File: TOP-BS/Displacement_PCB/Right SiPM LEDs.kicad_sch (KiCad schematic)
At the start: 36 parts

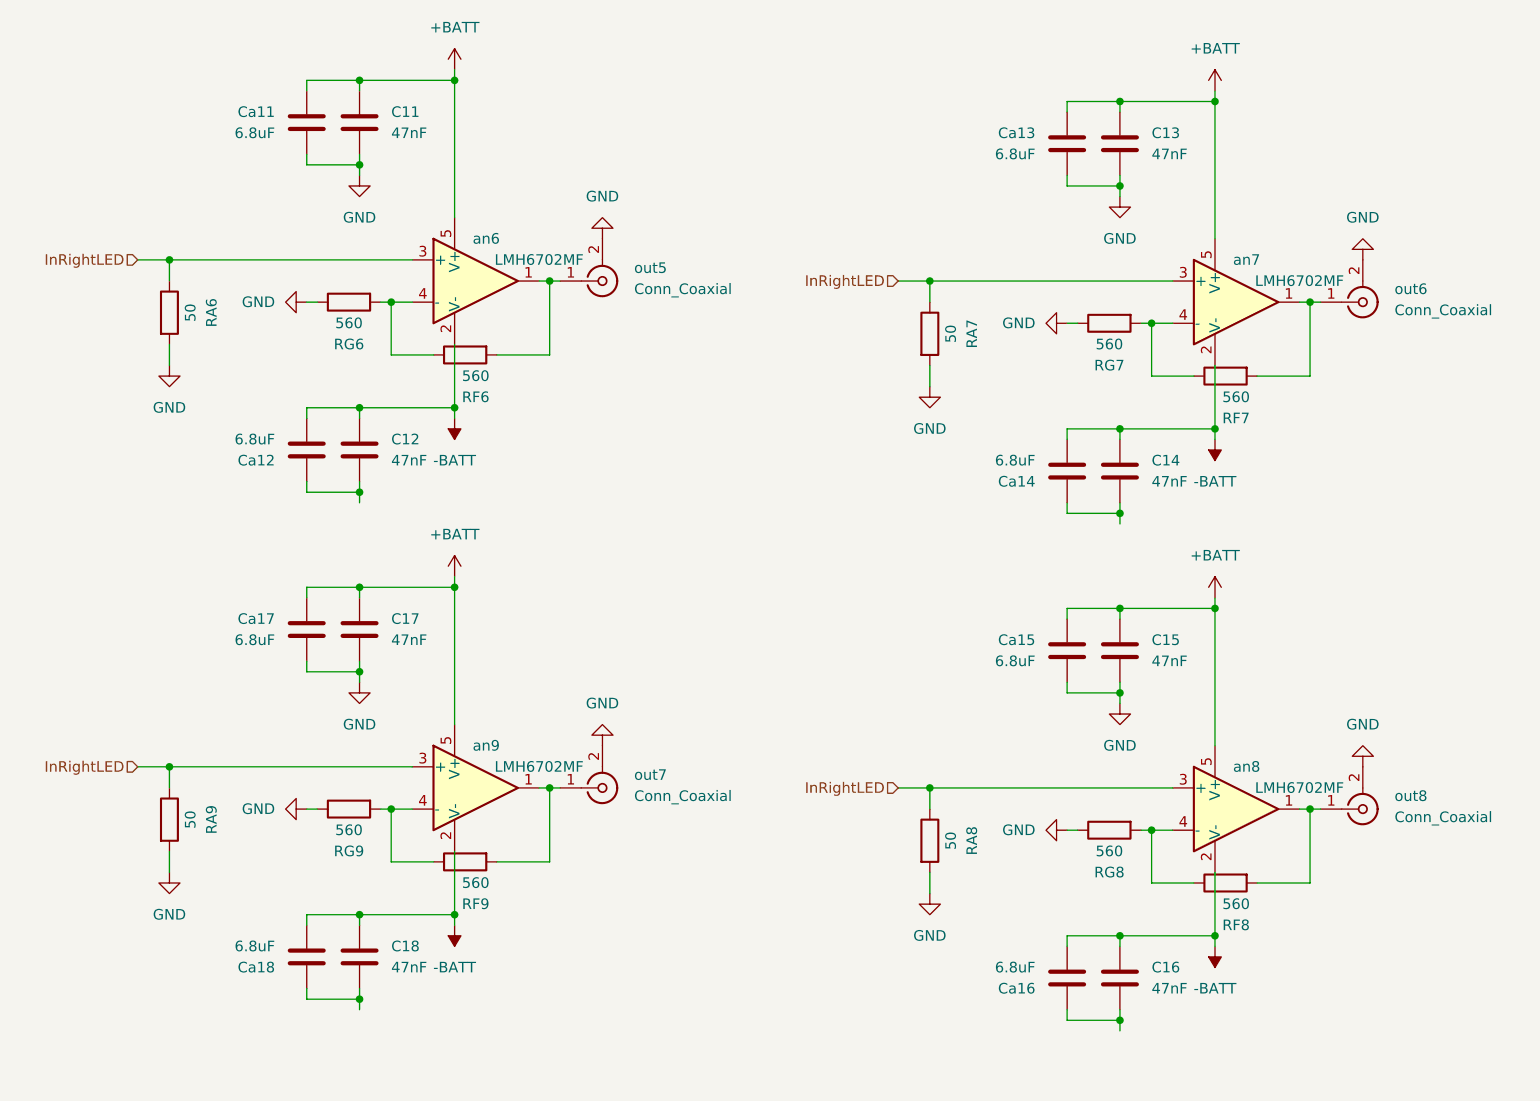
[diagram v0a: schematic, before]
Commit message: Updated Distribution PCB sch
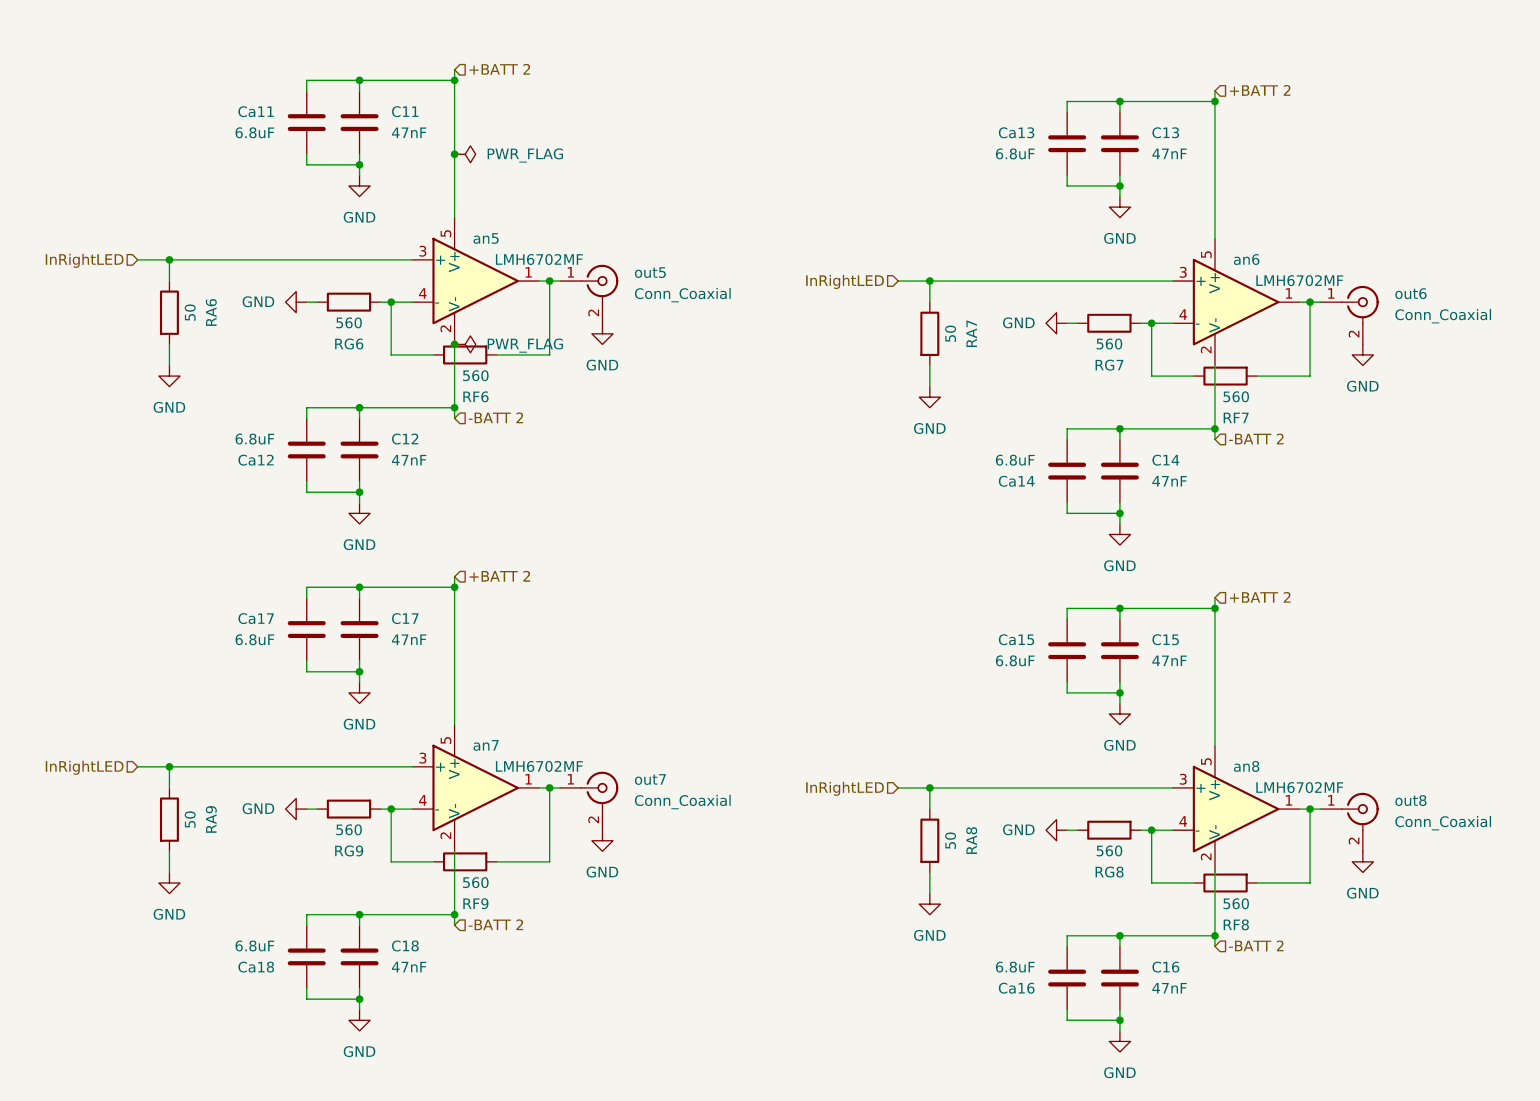
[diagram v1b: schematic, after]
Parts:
- renumbered an6 to an5, an7 to an6, an9 to an7
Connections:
- net GND: now also C12.2, C14.2, C16.2, C18.2, Ca12.1, Ca14.1, Ca16.1, Ca18.1
- net +BATT renamed +BATT 2
- net -BATT renamed -BATT 2
